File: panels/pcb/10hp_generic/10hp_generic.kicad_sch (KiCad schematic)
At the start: 89 parts, among them J1 CAN_PWR, J2 SWD, J3 I2C, SW1 SW_Push, SW10 SW_Push, SW11 SW_Push, SW12 SW_Push, SW13 SW_Push, SW14 SW_Push, SW15 SW_Push, SW16 SW_Push, SW2 SW_Push, SW3 SW_Push, SW4 SW_Push, SW5 SW_Push, SW6 SW_Push, SW7 SW_Push, SW8 SW_Push, SW9 SW_Push, U1 TJA1051T-3, U2 AMS1117-3.3, U3 STM32F103C8Tx, Y1 8MHz

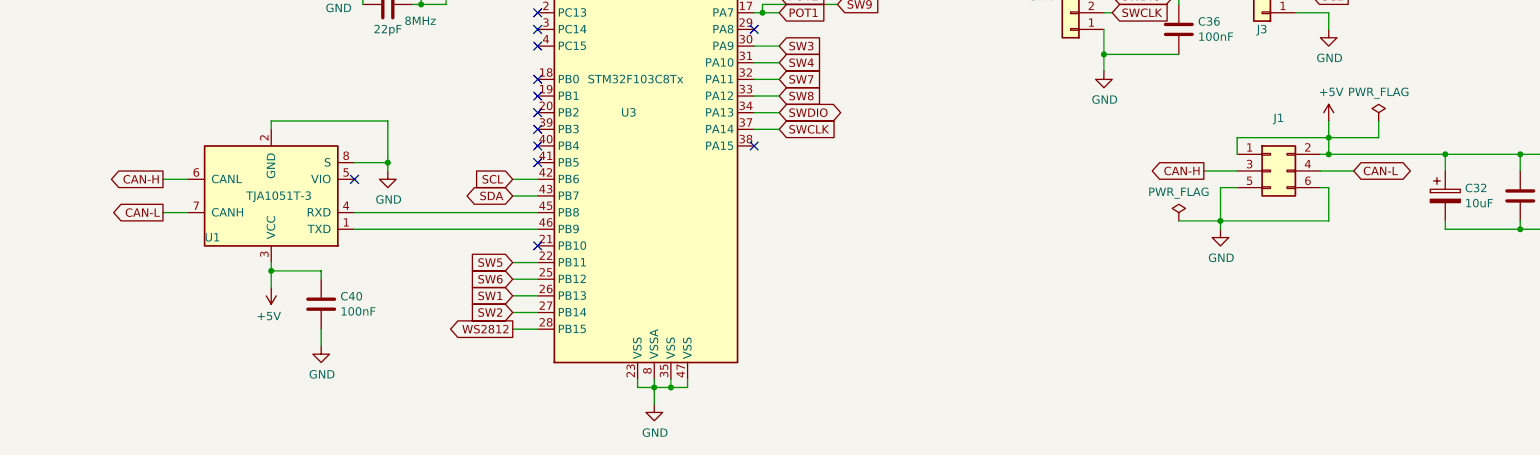
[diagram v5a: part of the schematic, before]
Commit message: Fixes to generic 10hp schematic and PCB
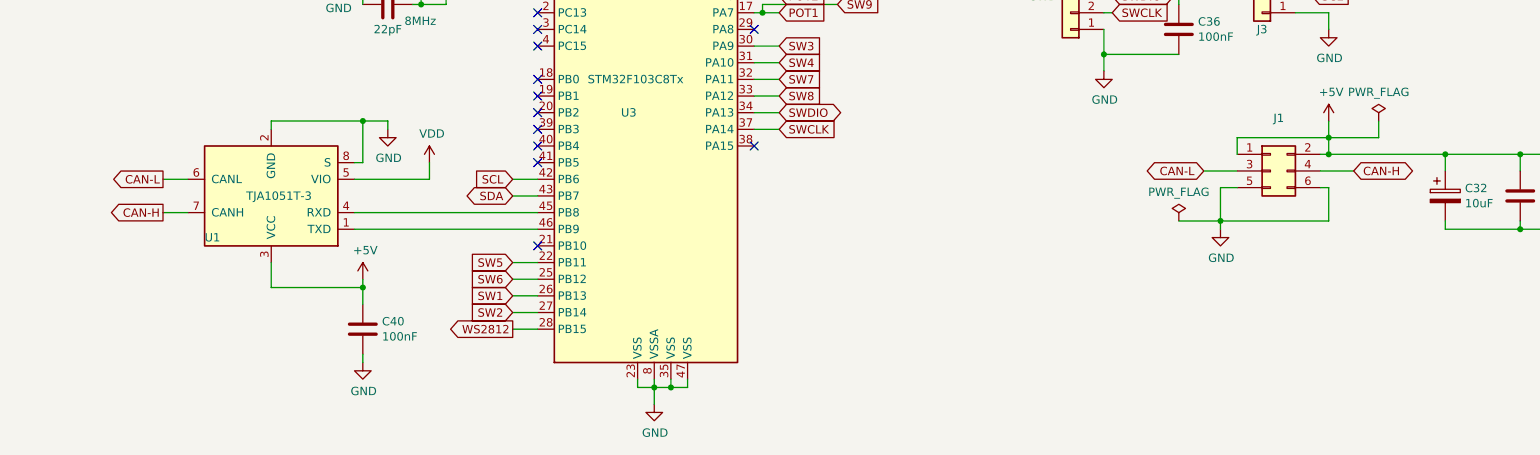
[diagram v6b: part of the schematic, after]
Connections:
- net CAN-H: now also J1.4 (Pin_4), U1.7 (CANH); no longer J1.3 (Pin_3), U1.6 (CANL)
- net CAN-L: now also J1.3 (Pin_3), U1.6 (CANL); no longer J1.4 (Pin_4), U1.7 (CANH)
- net VDD: now also U1.5 (VIO)
- no-connect marks 14 -> 13
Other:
- moved on the sheet: C40
